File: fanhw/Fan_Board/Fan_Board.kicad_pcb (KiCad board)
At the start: 2 copper layers, 56.5 x 29.5 mm, 36 parts, among them J1 USB_C_Receptacle_PowerOnly_6P, J2 Conn_01x05_Female, J3 Screw_Terminal_01x02, Q1 T2N7002AK, SW1 Power Switch, U1 TLV61046ADB, U2 PIC18F26K83-xSP

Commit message: Small edits, production files
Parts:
- removed H4: MountingHole_Pad, MountingHole:MountingHole_3.2mm_M3_DIN965_Pad
- moved H3 5.84 mm to (159.9, 61.8)
- moved R10 0.28 mm to (144.7, 72.5)
- moved R9 0.13 mm to (144.7, 75.7)
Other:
- board size 56.5 x 29.5 mm -> 50.7 x 29.5 mm
- board text added: "To blow or not to blow, that is the question. Darien Ng"
- board text removed: "Fan go brr"

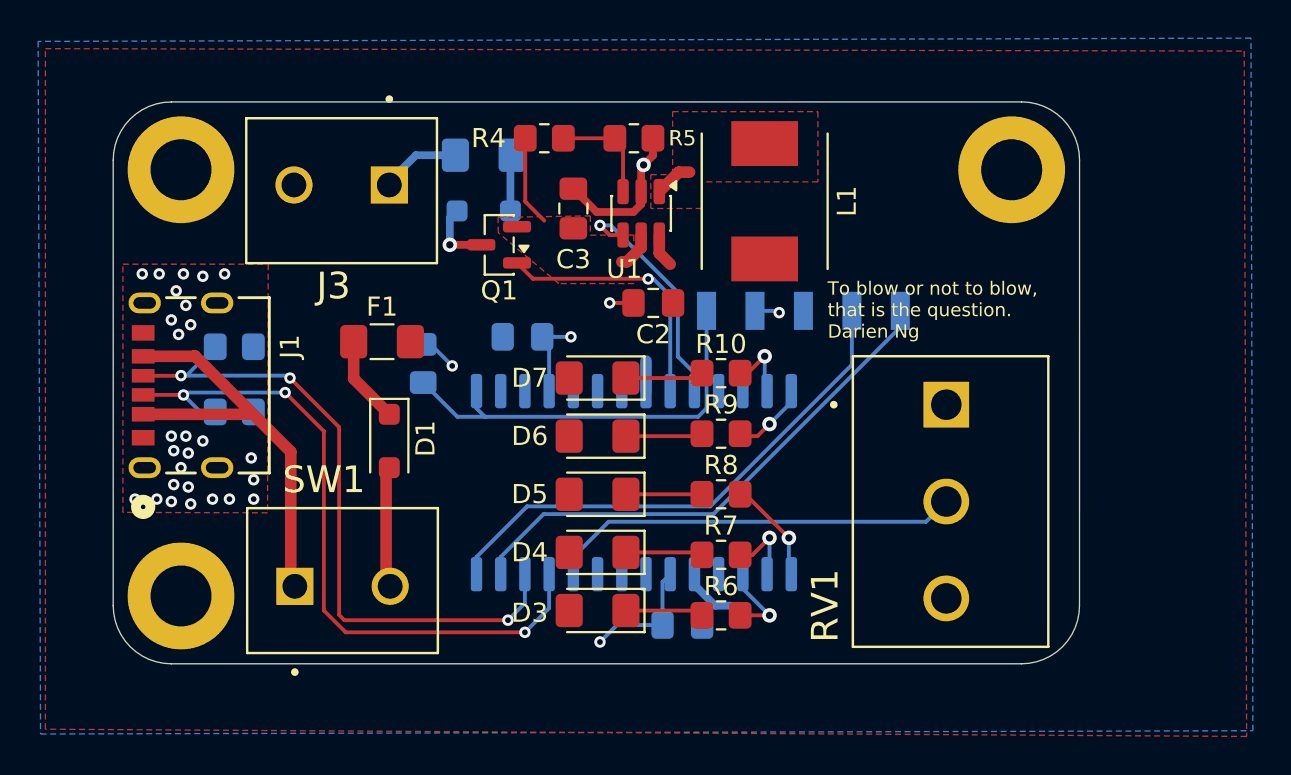
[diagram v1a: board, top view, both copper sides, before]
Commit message: added oscillator, regen prod files
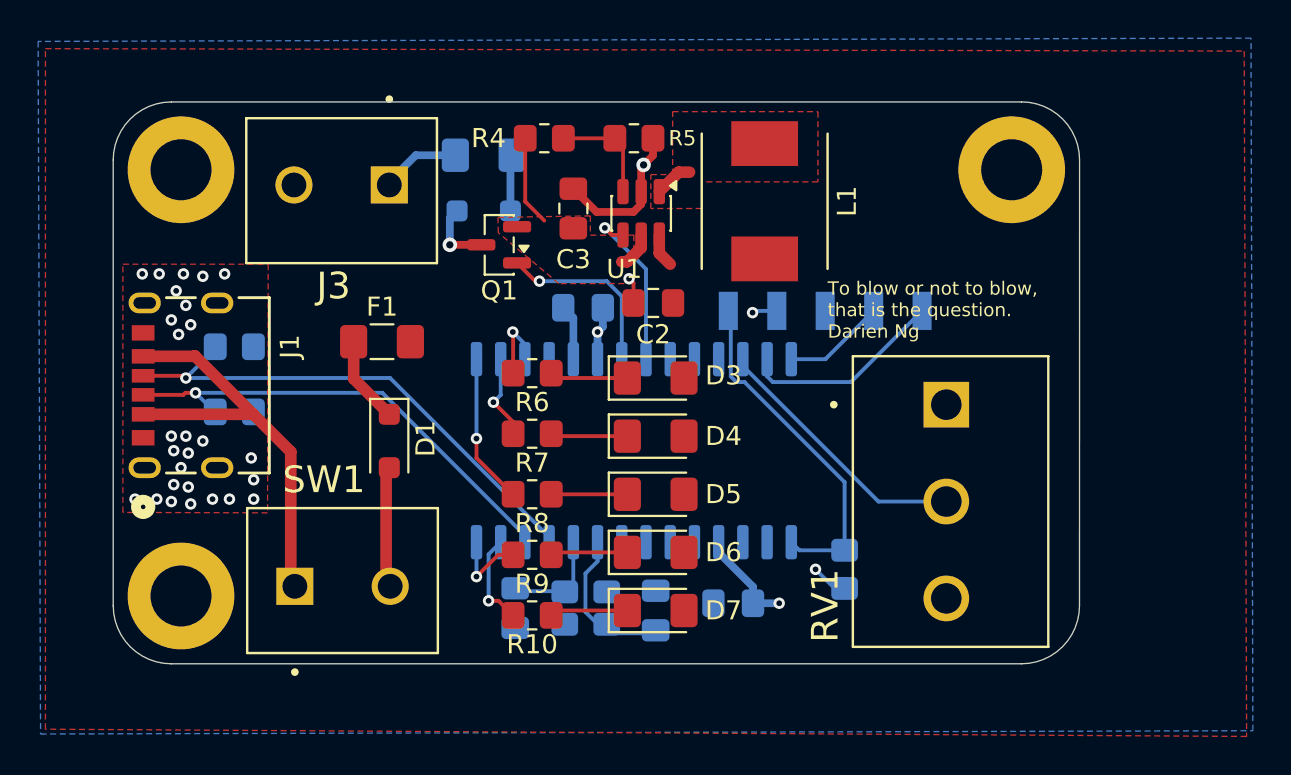
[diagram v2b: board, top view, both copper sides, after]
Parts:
- added C10: 26pF, Capacitor_SMD:C_0805_2012Metric_Pad1.18x1.45mm_HandSolder, B.Cu at (133.9, 84.8)
- added C9: 26pF, Capacitor_SMD:C_0805_2012Metric_Pad1.18x1.45mm_HandSolder, B.Cu at (141.2, 85.0)
- added Y1: ABM8G-12.000MHZ-18-D2Y-T, Crystal:Crystal_SMD_Abracon_ABM8G-4Pin_3.2x2.5mm, B.Cu at (137.6, 84.8)
- moved R22 24.6 mm to (151.1, 82.8), turned to -90 degrees
- moved R10 16.1 mm to (134.7, 85.2), turned to 180 degrees
- moved R6 16.1 mm to (134.7, 72.5), turned to 180 degrees
- moved D3 12.6 mm to (141.2, 72.8), turned to 0 degrees
- moved D7 12.6 mm to (141.2, 85.0), turned to 0 degrees
- moved R7 11.8 mm to (134.7, 75.7), turned to 180 degrees
- moved R9 11.8 mm to (134.7, 82.0), turned to 180 degrees
- moved R8 9.91 mm to (134.7, 78.9), turned to 180 degrees
- moved D4 6.82 mm to (141.2, 75.8), turned to 0 degrees
- moved D6 6.82 mm to (141.2, 81.9), turned to 0 degrees
- moved C5 3.52 mm to (137.4, 69.1)
- moved D5 3.05 mm to (141.2, 78.9), turned to 0 degrees
- moved C4 2.90 mm to (145.3, 84.6), turned to 180 degrees
- moved U2 1.68 mm to (140.1, 76.6), turned to 90 degrees
- moved J2 1.14 mm to (155.2, 69.2)
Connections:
- U2 pad 10: /Fan Power/Boost_EN -> /MCU/OSC2
- U2 pad 11: unconnected-(U2-RC0/SOSCO-Pad11) -> /CC2
- U2 pad 12: unconnected-(U2-RC1/SOSCI-Pad12) -> /CC1
- U2 pad 21: unconnected-(U2-RB0-Pad21) -> /Fan Power/FAN_GATE
- U2 pad 22: unconnected-(U2-RB1-Pad22) -> /Fan Power/Boost_EN
- U2 pad 24: /MCU/POT -> unconnected-(U2-RB3-Pad24)
- U2 pad 25: /CC1 -> unconnected-(U2-RB4-Pad25)
- U2 pad 26: /CC2 -> /MCU/POT
- U2 pad 9: /Fan Power/FAN_GATE -> /MCU/OSC1
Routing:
- net /MCU/ICSPDAT: track 27.6 -> 5.37 mm
- net /MCU/ICSPCLK: track 27.7 -> 10.7 mm
- net /CC1: track 36.4 -> 25.0 mm, vias 3 -> 1
- net /CC2: track 36.3 -> 27.3 mm, vias 3 -> 1
- net /MCU/OSC1: track 0.00 -> 8.13 mm
- net /MCU/POT: track 21.7 -> 14.0 mm
- net /MCU/OSC2: track 0.00 -> 5.59 mm
- net /Fan Power/FAN_GATE: track 13.8 -> 9.51 mm
- net /MCU/~{MCLR}: track 22.5 -> 18.3 mm
- net /Fan Power/Boost_EN: track 12.5 -> 8.89 mm
- net +5V: track 16.0 -> 13.1 mm
- net /MCU/LED3: track 5.46 -> 7.89 mm
- net GND: track 14.2 -> 12.2 mm
- net /MCU/LED5: track 3.54 -> 4.94 mm
- net /MCU/LED2: track 3.87 -> 4.50 mm
